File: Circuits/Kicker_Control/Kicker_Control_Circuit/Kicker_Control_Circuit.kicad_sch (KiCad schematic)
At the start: 1 part, among them P1 66200621124

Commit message: kicker circuit changest
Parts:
- removed P1: 66200621124, Altium_WR-MPC3 (rev23a):66200621124, symbol WR-MPC3 3.00 mm Male Header Dual Row Vertical - THT:66200621124
- added 300VJ4: Conn_01x01_Pin, Connector_PinHeader_2.54mm:PinHeader_1x01_P2.54mm_Vertical, symbol Connector:Conn_01x01_Pin
- added C1: 0.1u, Capacitor_SMD:C_1812_4532Metric, symbol B32671P6104K000:B32671P6104K000
- added C2: 0.1u, Capacitor_SMD:C_1206_3216Metric, symbol B32671P6104K000:B32671P6104K000
- added C3: 1u, Capacitor_SMD:C_1206_3216Metric, symbol B32671P6104K000:B32671P6104K000
- added D1: Diode, Diode_SMD:D_SMC, symbol TVS_Diod_1.5SMC440A:Diode
- added IC1: UCC27511DBVR, IKB40N65ES5ATMA1 IGBT:BTS141TCBUMA1, symbol UCC27511DBVR:UCC27511DBVR
- added J3: Conn_01x03_Pin, Connector_PinHeader_2.54mm:PinHeader_1x03_P2.54mm_Vertical, symbol Connector:Conn_01x03_Pin
- added Q2: IKB40N65ES5ATMA1, IKB40N65ES5ATMA1 IGBT:BTS141TCBUMA1, symbol IKB40N65ES5ATMA1:IKB40N65ES5ATMA1
- added R1: 10k, Resistor_SMD:R_1210_3225Metric, symbol CRCW121010K0JNEAIF:CRCW121010K0JNEAIF
- added R2, R3: 10k, Resistor_SMD:R_1210_3225Metric, symbol Device:R
- added R4: 100, Resistor_SMD:R_2010_5025Metric, symbol Device:R
- added Solenoid+1: Solenoid-, Connector_PinHeader_2.54mm:PinHeader_1x02_P2.54mm_Vertical, symbol Connector:Conn_01x02_Pin
- added U2: VS-5EWH06FN-M3, VS-5EWH06FN-M3:DPAK_06FN-M3_VIS, symbol VS-5EWH06FN-M3:VS-5EWH06FN-M3
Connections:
- new net: R1.1, R2.2, R3.2, R4.1
- new net: C1.1, D1.2 (C), Q2.1 (G), R4.2
- new net: IC1.2 (OUTH), R3.1
- new net: IC1.3 (OUTL), R2.1
- new net 15V: C2.1, C3.1, IC1.1 (VDD), J3.3 (Pin_3)
- new net GND: C1.2, C2.2, C3.2, D1.1 (A), IC1.4 (GND), IC1.5 (IN-), J3.1 (Pin_1), Q2.3 (E), R1.2
- new net On_Signal 3V: IC1.6 (IN+), J3.2 (Pin_2)
- new net Output1_Solenoid : 300VJ4.1 (Pin_1), Solenoid+1.2 (Pin_2), U2.2
- new net Output2_Solenoid : Q2.2 (C), Solenoid+1.1 (Pin_1), U2.3
- no-connect marks 0 -> 1
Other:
- removed sheet LT3751 Capacitor Charger

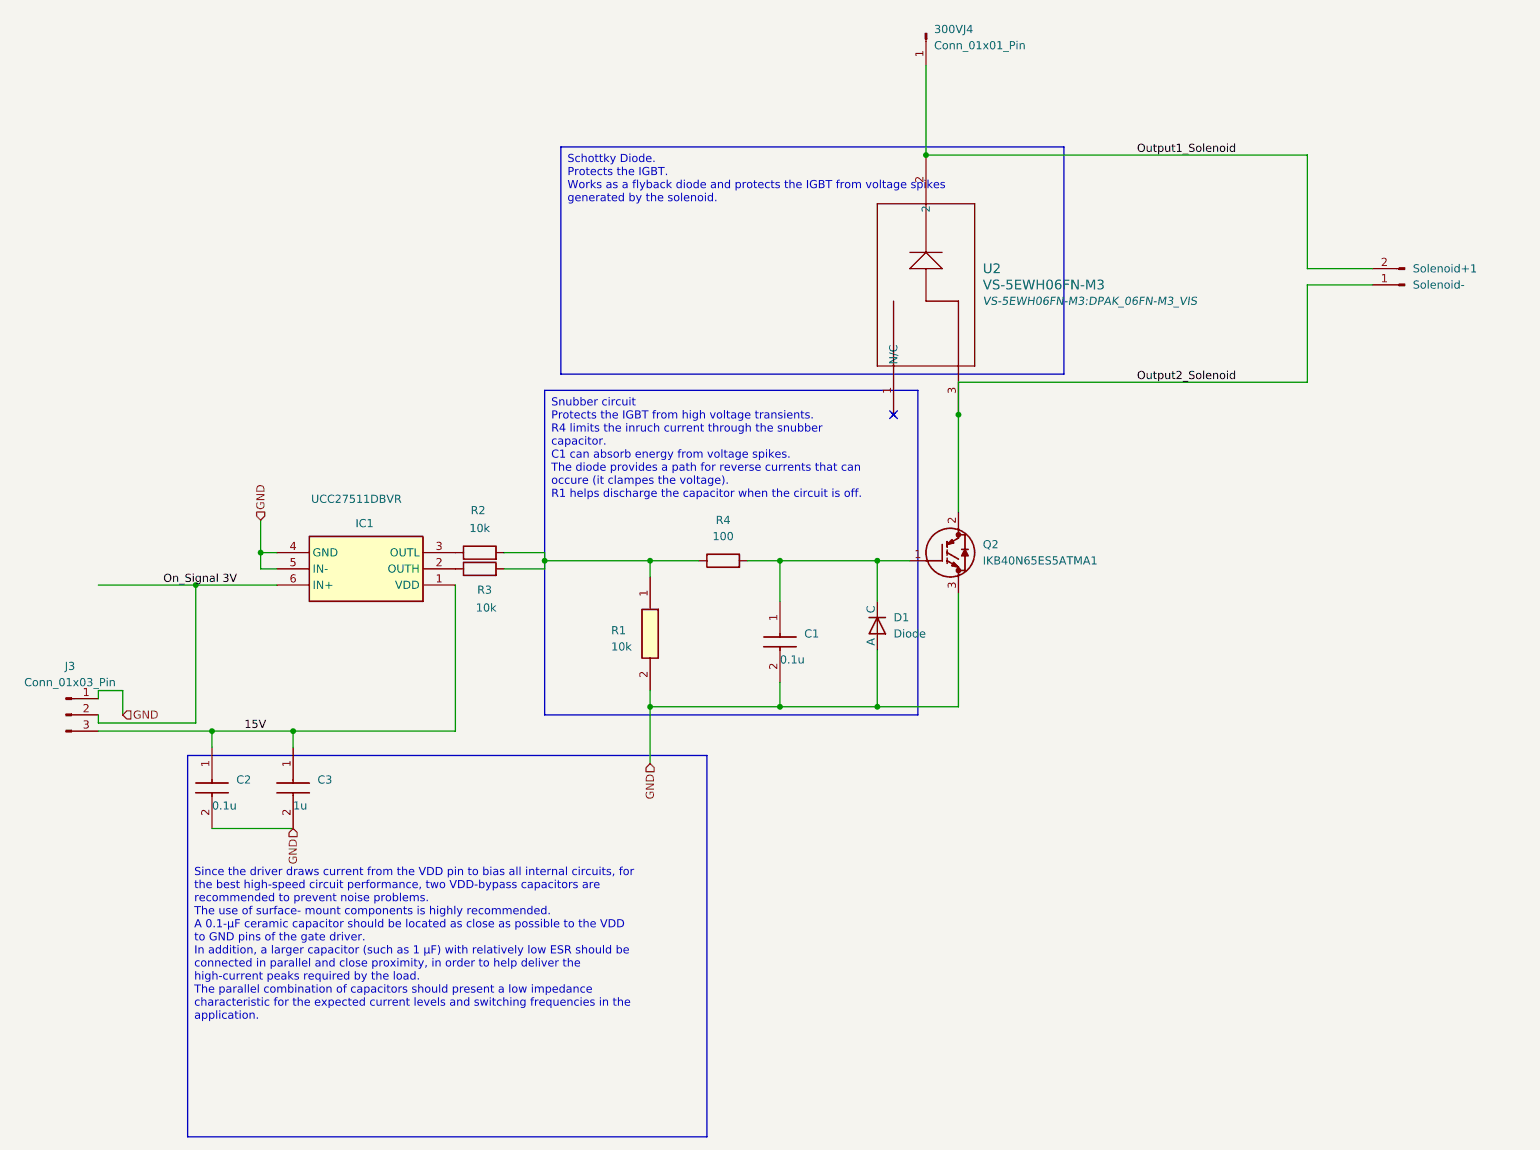
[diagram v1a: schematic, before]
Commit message: Updated the capacitor footprints to 0805, since everyone was different. Added powerplane and groundplane, vias for ground connections, added a connector to for the solenoid to a 1x2 pin headers since those are easier to find. Changed the connections for the output1_solenoid and outpu2_solenoid to have separate connectors, maybe not necessary
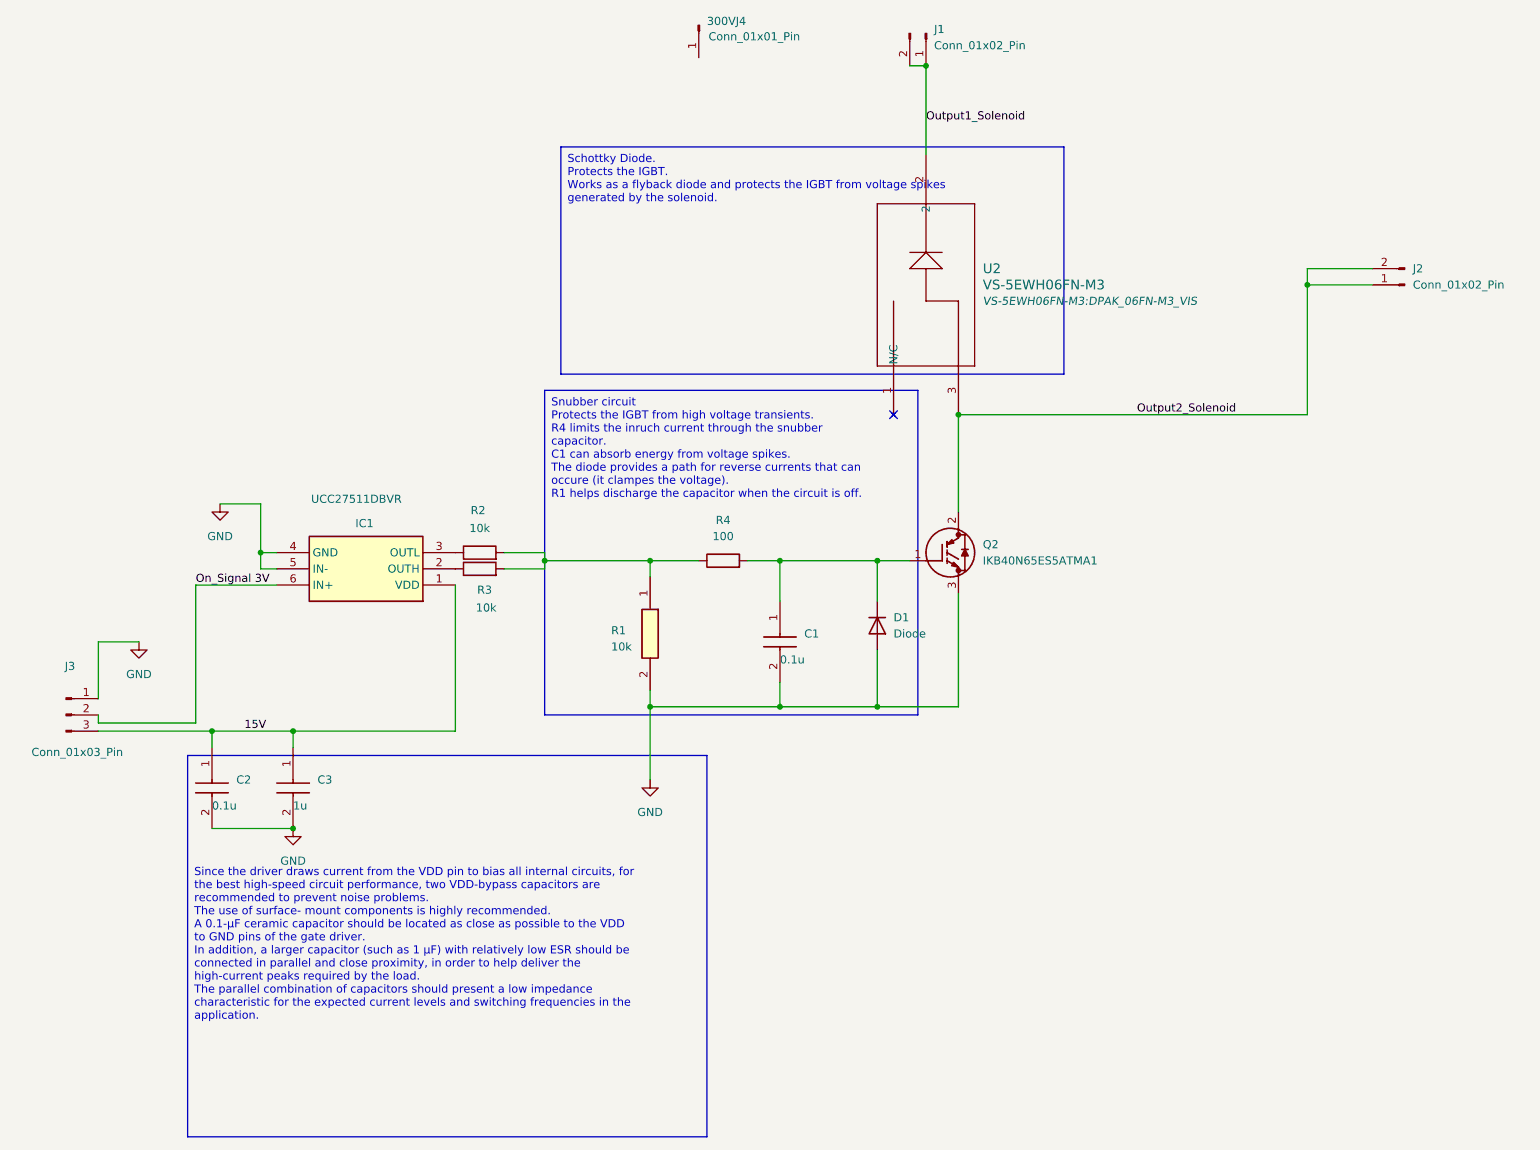
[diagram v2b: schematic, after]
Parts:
- added J1: Conn_01x02_Pin, Connector_PinHeader_2.54mm:PinHeader_1x02_P2.54mm_Vertical, symbol Connector:Conn_01x02_Pin
- C1: footprint Capacitor_SMD:C_1812_4532Metric -> Capacitor_SMD:C_0805_2012Metric_Pad1.18x1.45mm_HandSolder
- C2, C3: footprint Capacitor_SMD:C_1206_3216Metric -> Capacitor_SMD:C_0805_2012Metric_Pad1.18x1.45mm_HandSolder
- D1: symbol TVS_Diod_1.5SMC440A:Diode -> Device:D
- J2: renamed from Solenoid+1; value Solenoid- -> Conn_01x02_Pin
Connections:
- net GND: now also D1.2 (A); no longer D1.1 (A)
- net Output1_Solenoid : now also J1.1 (Pin_1), J1.2 (Pin_2); no longer 300VJ4.1 (Pin_1), J2.2 (Pin_2)
- net Output2_Solenoid : now also J2.2 (Pin_2)
- net at C1.1, Q2.1 (G), R4.2: now also D1.1 (K); no longer D1.2 (C)
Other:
- moved on the sheet: 300VJ4

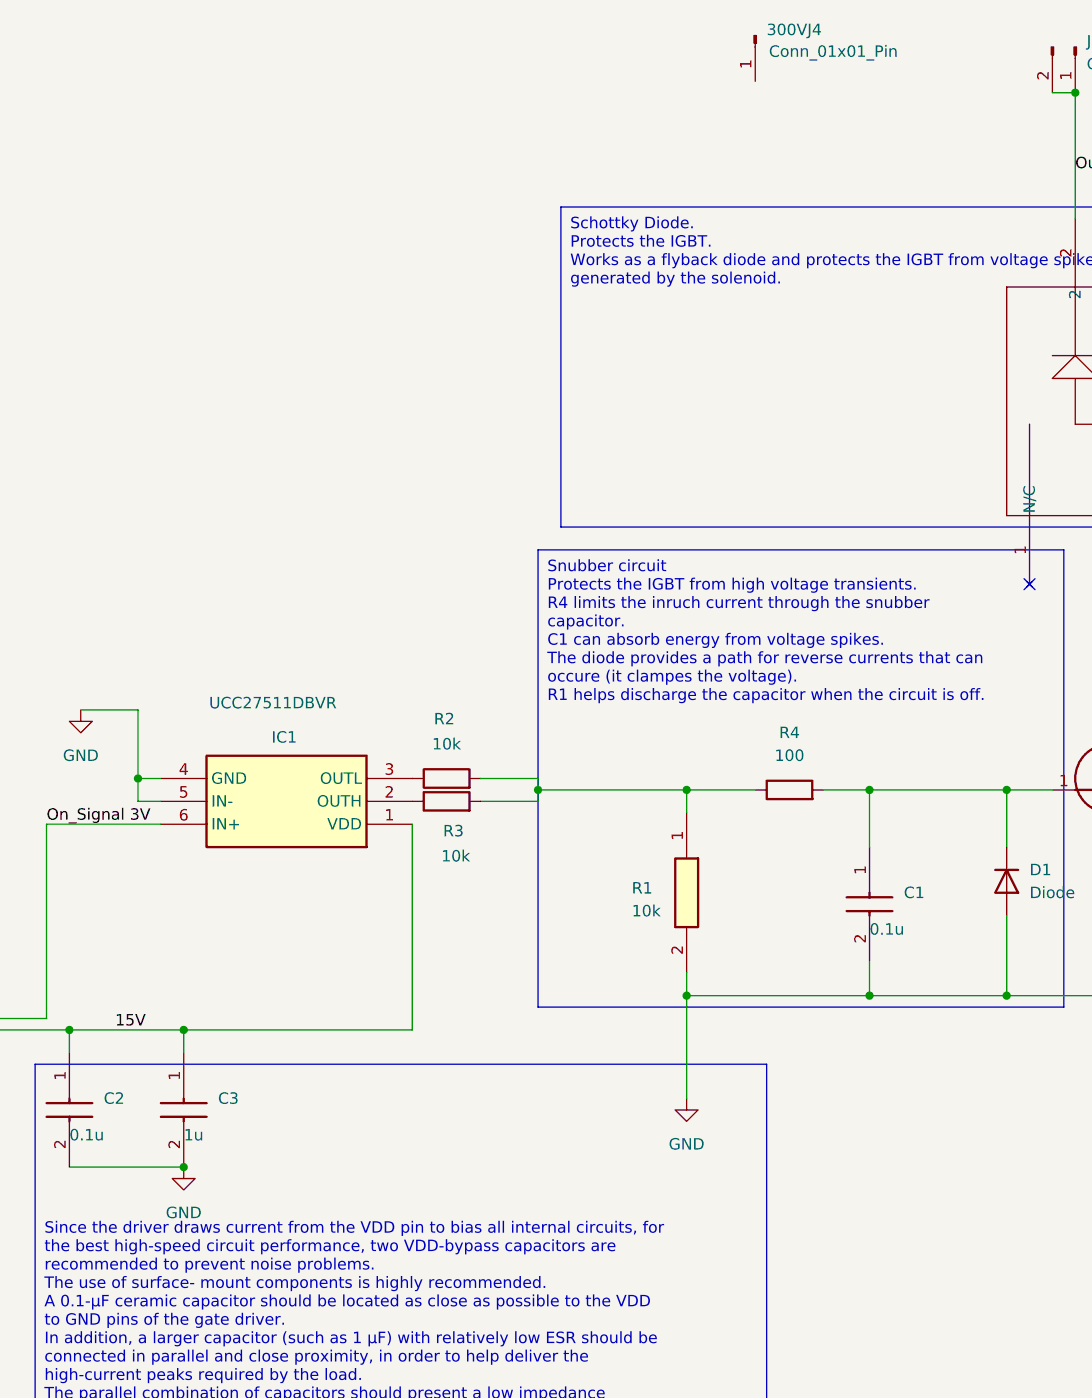
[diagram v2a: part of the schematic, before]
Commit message: Deleted unnecessary files
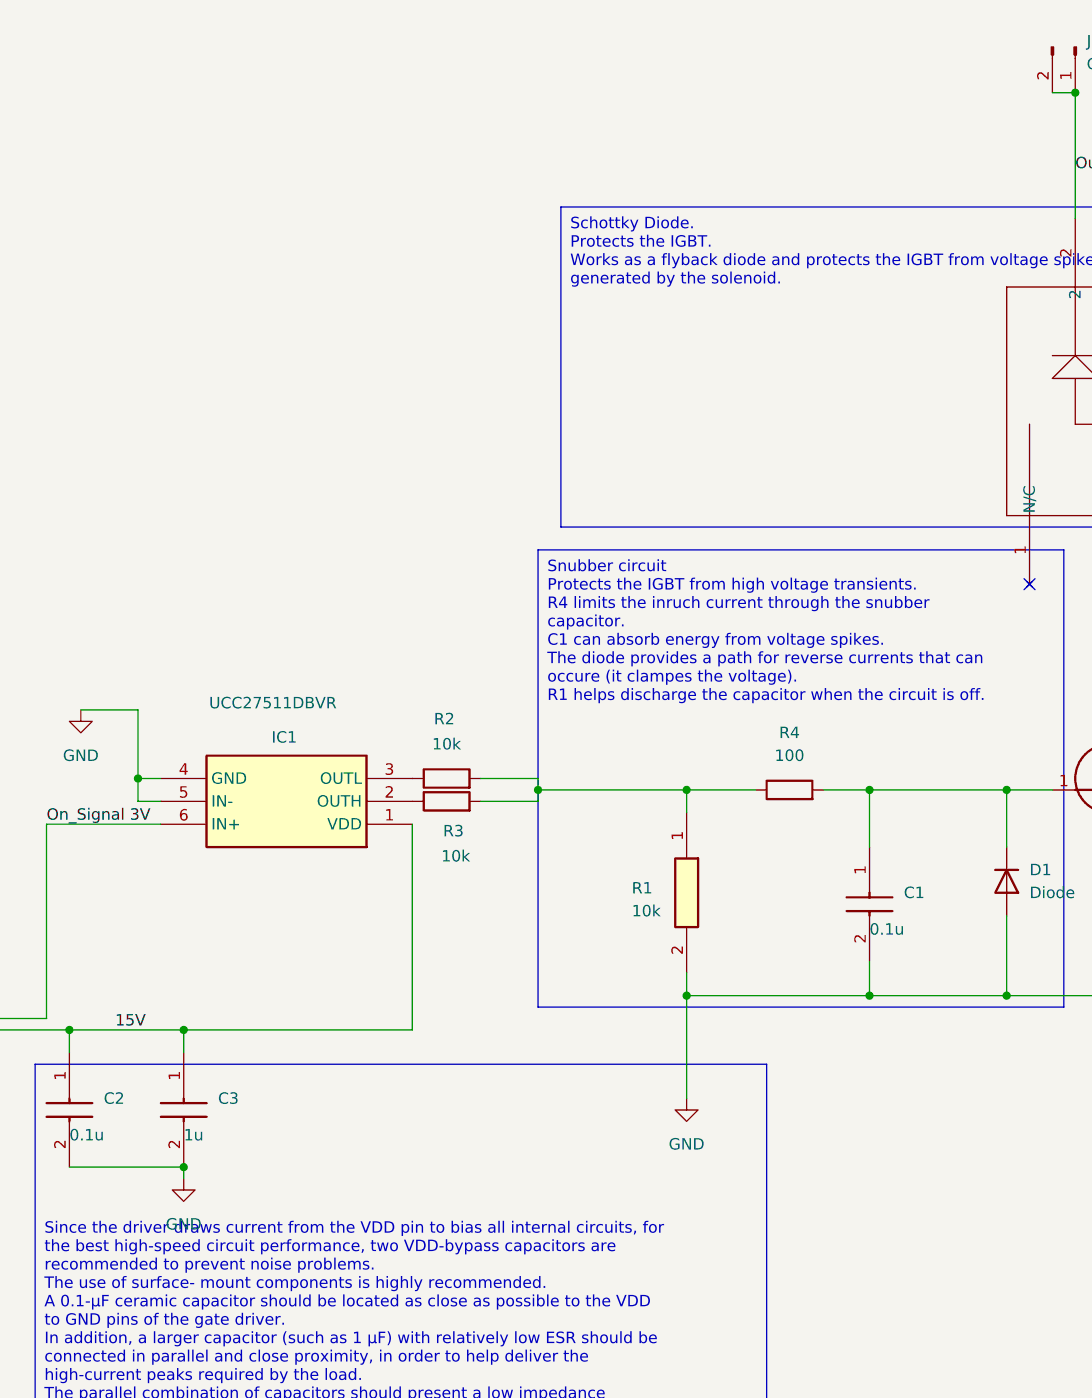
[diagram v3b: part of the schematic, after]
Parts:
- removed 300VJ4: Conn_01x01_Pin, Connector_PinHeader_2.54mm:PinHeader_1x01_P2.54mm_Vertical, symbol Connector:Conn_01x01_Pin
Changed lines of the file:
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@@
+	(wire
+		(pts
+			(xy 87.63 143.51) (xy 87.63 142.24)
+		)
+		(stroke
+			(width 0)
+			(type default)
+		)
+	)
 	(wire
 		(pts
@@
 	)
 	(symbol
-		(lib_id "Connector:Conn_01x01_Pin")
-		(at 151.13 16.51 270)
-		(unit 1)
-		(exclude_from_sim no)
-		(in_bom yes)
-		(on_board no)
-		(dnp no)
-		(property "Reference" "300VJ4"
-			(at 152.4 15.8749 90)
-			(effects
-				(font
-					(size 1.27 1.27)
-				)
-				(justify left)
-			)
-		)
-		(property "Value" "Conn_01x01_Pin"
-			(at 152.654 18.288 90)
-			(effects
-				(font
-					(size 1.27 1.27)
-				)
-				(justify left)
-			)
-		)
-		(property "Footprint" "Connector_PinHeader_2.54mm:PinHeader_1x01_P2.54mm_Vertical"
-			(at 151.13 16.51 0)
-			(effects
-				(font
-					(size 1.27 1.27)
-				)
-				(hide yes)
-			)
-		)
-		(property "Datasheet" "~"
-			(at 151.13 16.51 0)
-			(effects
-				(font
-					(size 1.27 1.27)
-				)
-				(hide yes)
-			)
-		)
-		(property "Description" "Generic connector, single row, 01x01, script generated"
-			(at 151.13 16.51 0)
-			(effects
-				(font
-					(size 1.27 1.27)
-				)
-				(hide yes)
-			)
-		)
-		(pin "1"
-		)
-		(instances
-			(project ""
-				(path "/58552bde-dccf-45b1-8fa9-001877e59e11"
-					(reference "300VJ4")
-					(unit 1)
-				)
-			)
-		)
-	)
-	(symbol
 		(lib_id "Device:D")
 		(at 179.07 110.49 270)
@@
 	(symbol
 		(lib_id "power:GND")
-		(at 87.63 142.24 0)
+		(at 87.63 143.51 0)
 		(unit 1)
 		(exclude_from_sim no)
@@
 		(fields_autoplaced yes)
 		(property "Reference" "#PWR01"
+			(at 87.63 149.86 0)
+			(effects
+				(font
+					(size 1.27 1.27)
+				)
+				(hide yes)
+			)
+		)
+		(property "Value" "GND"
 			(at 87.63 148.59 0)
 			(effects
@@
 					(size 1.27 1.27)
 				)
-				(hide yes)
-			)
-		)
-		(property "Value" "GND"
-			(at 87.63 147.32 0)
-			(effects
-				(font
-					(size 1.27 1.27)
-				)
 			)
 		)
 		(property "Footprint" ""
-			(at 87.63 142.24 0)
+			(at 87.63 143.51 0)
 			(effects
 				(font
@@
 		)
 		(property "Datasheet" ""
-			(at 87.63 142.24 0)
+			(at 87.63 143.51 0)
 			(effects
 				(font
@@
 		)
 		(property "Description" "Power symbol creates a global label with name \"GND\" , ground"
-			(at 87.63 142.24 0)
-			(effects
-				(font
+			(at 87.63 143.51 0)
+			(effects
+				(font
